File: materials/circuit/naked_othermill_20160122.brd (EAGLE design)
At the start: 52.1 x 59.7 mm, 20 parts, among them IC1 LM358N

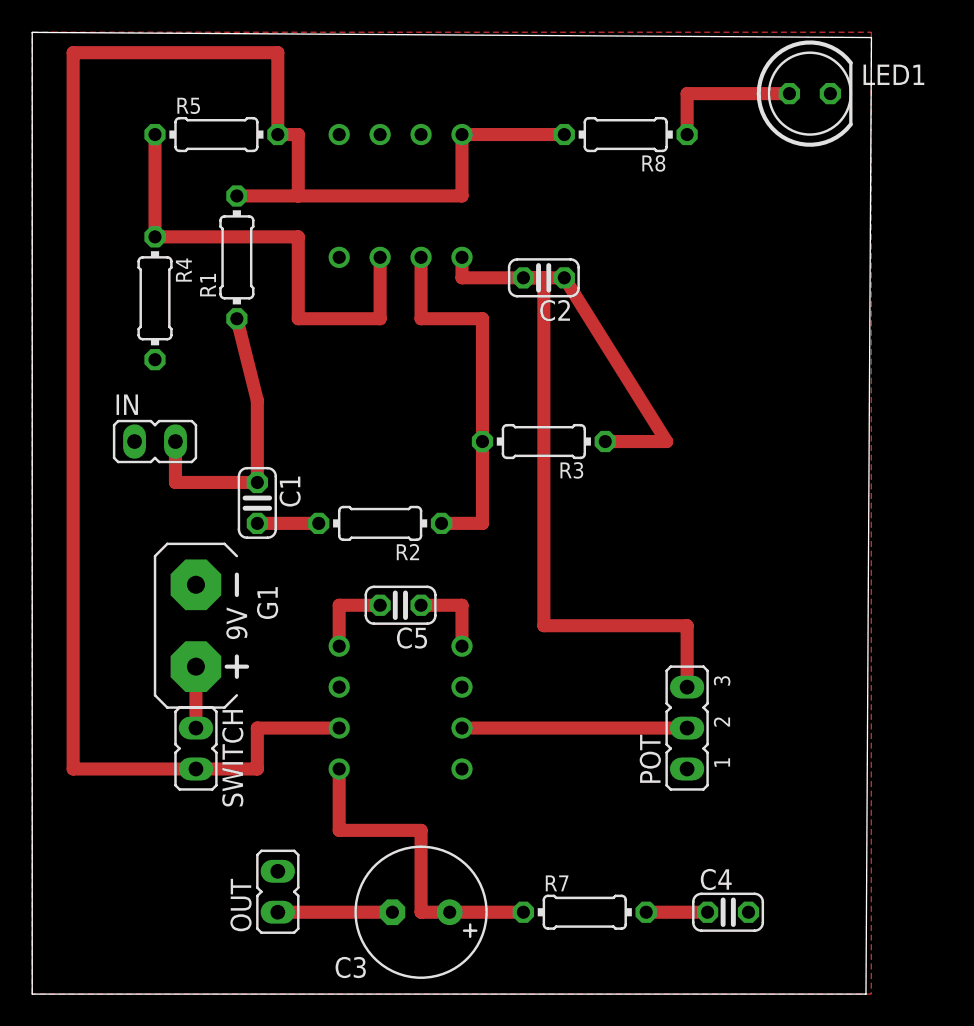
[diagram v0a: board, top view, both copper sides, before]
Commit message: updated online resources
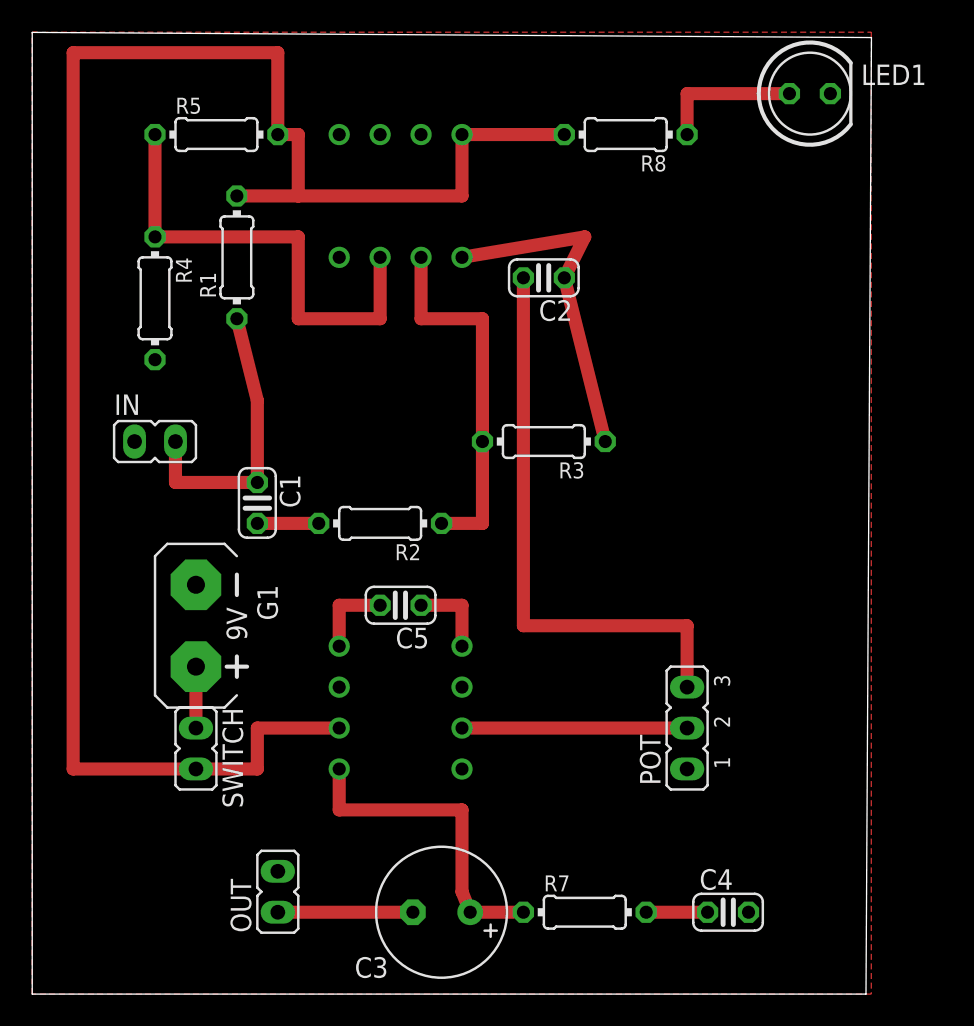
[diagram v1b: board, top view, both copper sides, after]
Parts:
- moved C3 1.27 mm to (25.4, 5.08)
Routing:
- net N$7: track 23.4 -> 21.0 mm
- net N$11: track 7.11 -> 8.38 mm
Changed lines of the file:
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@@
 <element name="IN" library="jumper" package="JP1" value="" x="7.62" y="34.29" rot="R270"/>
 <element name="OUT" library="jumper" package="JP1" value="" x="15.24" y="6.35"/>
-<element name="C3" library="rcl" package="E3,5-8" value="220uF" x="24.13" y="5.08" rot="R180"/>
+<element name="C3" library="rcl" package="E3,5-8" value="220uF" x="25.4" y="5.08" rot="R180"/>
 </elements>
 <signals>
@@
 <contactref element="C2" pad="1"/>
 <contactref element="R3" pad="1"/>
-<wire x1="35.56" y1="34.29" x2="39.37" y2="34.29" width="0.8128" layer="1"/>
-<wire x1="39.37" y1="34.29" x2="33.02" y2="44.45" width="0.8128" layer="1"/>
-<wire x1="33.02" y1="44.45" x2="26.67" y2="44.45" width="0.8128" layer="1"/>
-<wire x1="26.67" y1="44.45" x2="26.67" y2="45.72" width="0.8128" layer="1"/>
+<wire x1="35.56" y1="34.29" x2="33.02" y2="44.45" width="0.8128" layer="1"/>
+<wire x1="33.02" y1="44.45" x2="34.29" y2="46.99" width="0.8128" layer="1"/>
+<wire x1="34.29" y1="46.99" x2="26.67" y2="45.72" width="0.8128" layer="1"/>
 </signal>
 <signal name="N$8">
 <contactref element="C2" pad="2"/>
 <contactref element="POT" pad="3"/>
-<wire x1="30.48" y1="44.45" x2="31.75" y2="44.45" width="0.8128" layer="1"/>
-<wire x1="31.75" y1="44.45" x2="31.75" y2="22.86" width="0.8128" layer="1"/>
-<wire x1="31.75" y1="22.86" x2="40.64" y2="22.86" width="0.8128" layer="1"/>
+<wire x1="30.48" y1="44.45" x2="30.48" y2="22.86" width="0.8128" layer="1"/>
+<wire x1="30.48" y1="22.86" x2="40.64" y2="22.86" width="0.8128" layer="1"/>
 <wire x1="40.64" y1="22.86" x2="40.64" y2="19.05" width="0.8128" layer="1"/>
 </signal>
@@
 <contactref element="R7" pad="1"/>
 <contactref element="C3" pad="+"/>
-<wire x1="25.908" y1="5.08" x2="30.48" y2="5.08" width="0.8128" layer="1"/>
-<wire x1="25.908" y1="5.08" x2="24.13" y2="5.08" width="0.8128" layer="1"/>
-<wire x1="24.13" y1="5.08" x2="24.13" y2="10.16" width="0.8128" layer="1"/>
-<wire x1="24.13" y1="10.16" x2="19.05" y2="10.16" width="0.8128" layer="1"/>
-<wire x1="19.05" y1="10.16" x2="19.05" y2="13.97" width="0.8128" layer="1"/>
+<wire x1="27.178" y1="5.08" x2="30.48" y2="5.08" width="0.8128" layer="1"/>
+<wire x1="27.178" y1="5.08" x2="26.67" y2="6.35" width="0.8128" layer="1"/>
+<wire x1="26.67" y1="6.35" x2="26.67" y2="11.43" width="0.8128" layer="1"/>
+<wire x1="26.67" y1="11.43" x2="19.05" y2="11.43" width="0.8128" layer="1"/>
+<wire x1="19.05" y1="11.43" x2="19.05" y2="13.97" width="0.8128" layer="1"/>
 </signal>
 <signal name="N$13">
@@
 <contactref element="C3" pad="-"/>
 <contactref element="OUT" pad="1"/>
-<wire x1="15.24" y1="5.08" x2="22.352" y2="5.08" width="0.8128" layer="1"/>
+<wire x1="15.24" y1="5.08" x2="23.622" y2="5.08" width="0.8128" layer="1"/>
 </signal>
 <signal name="N$3">
